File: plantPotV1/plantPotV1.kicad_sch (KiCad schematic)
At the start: 3 parts, among them U1 DS18B20

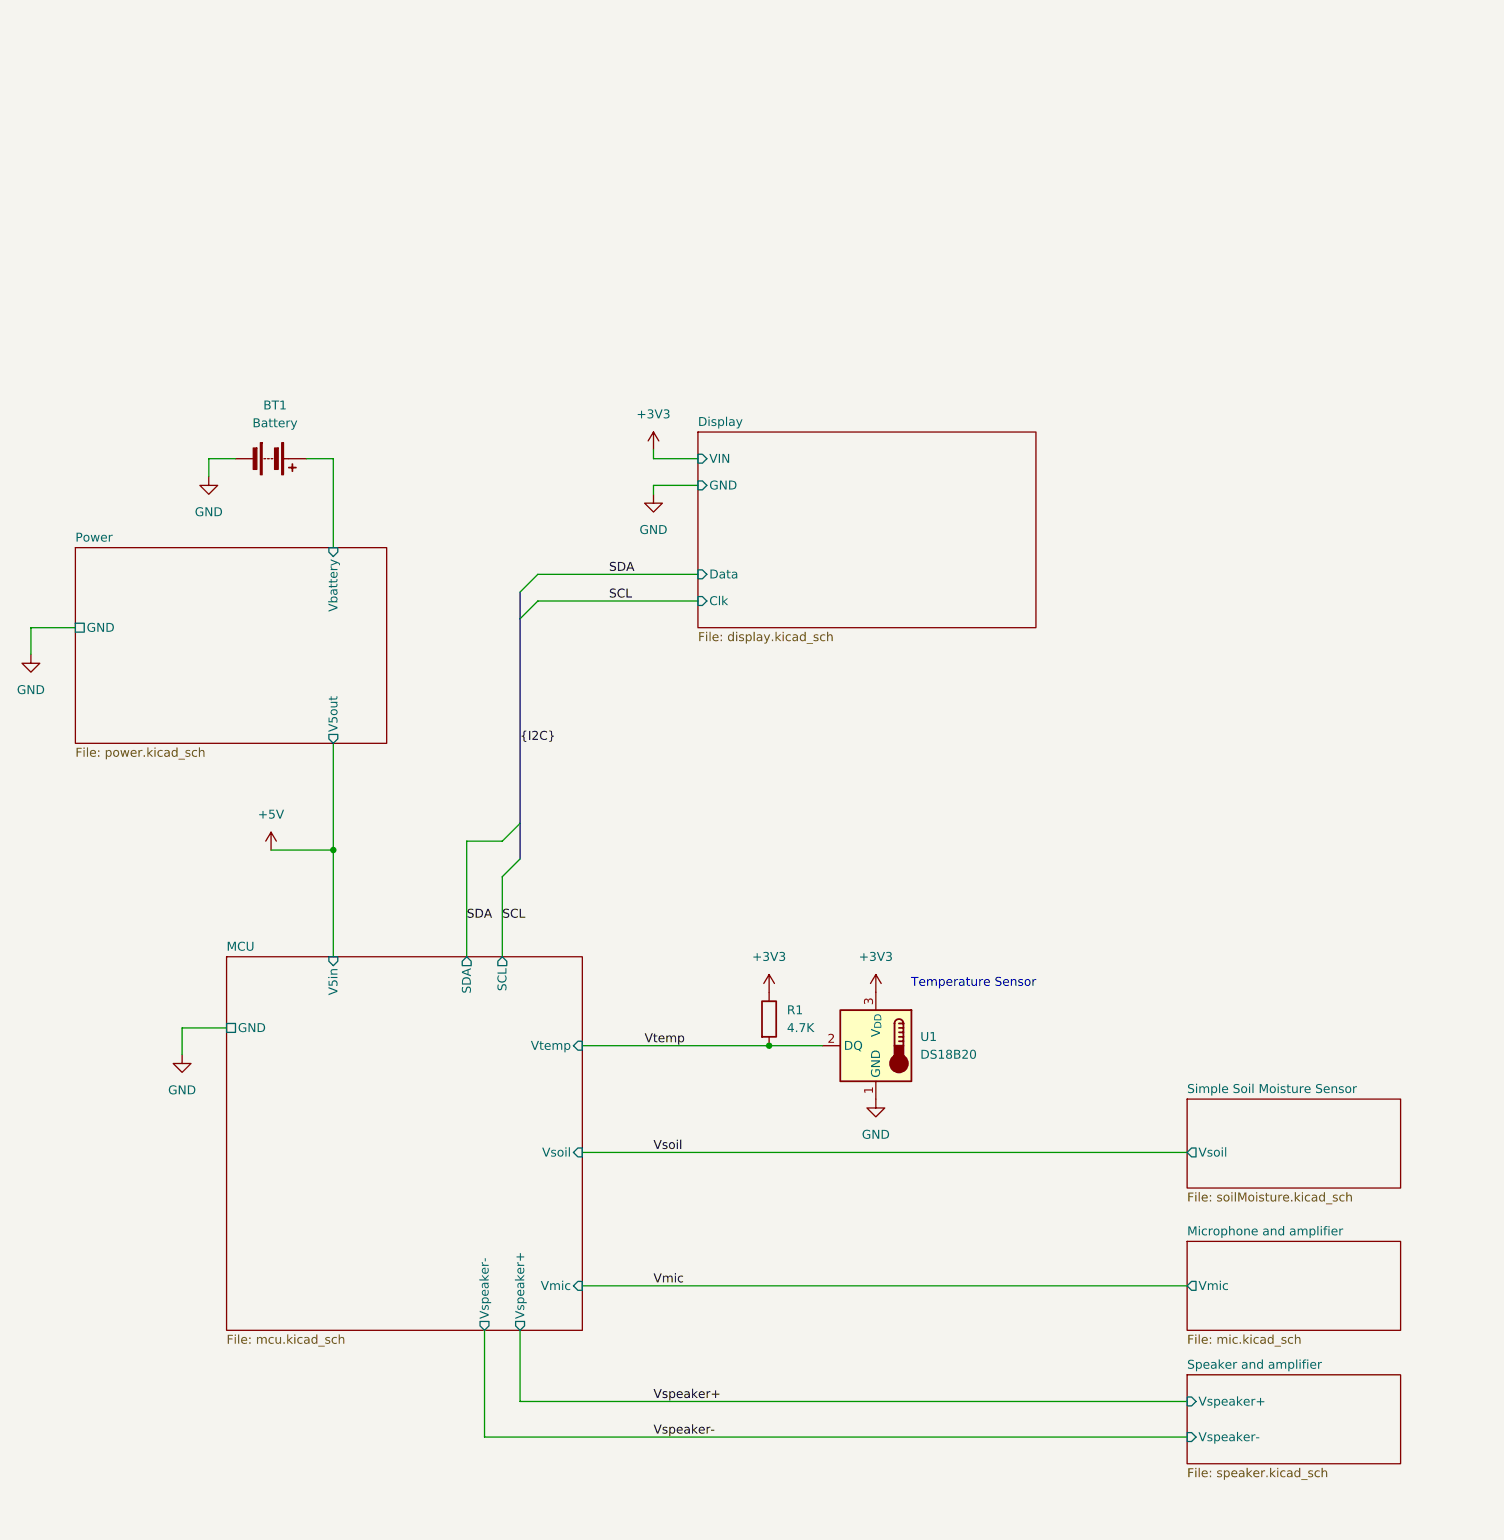
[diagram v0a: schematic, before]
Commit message: changed to meet proposal
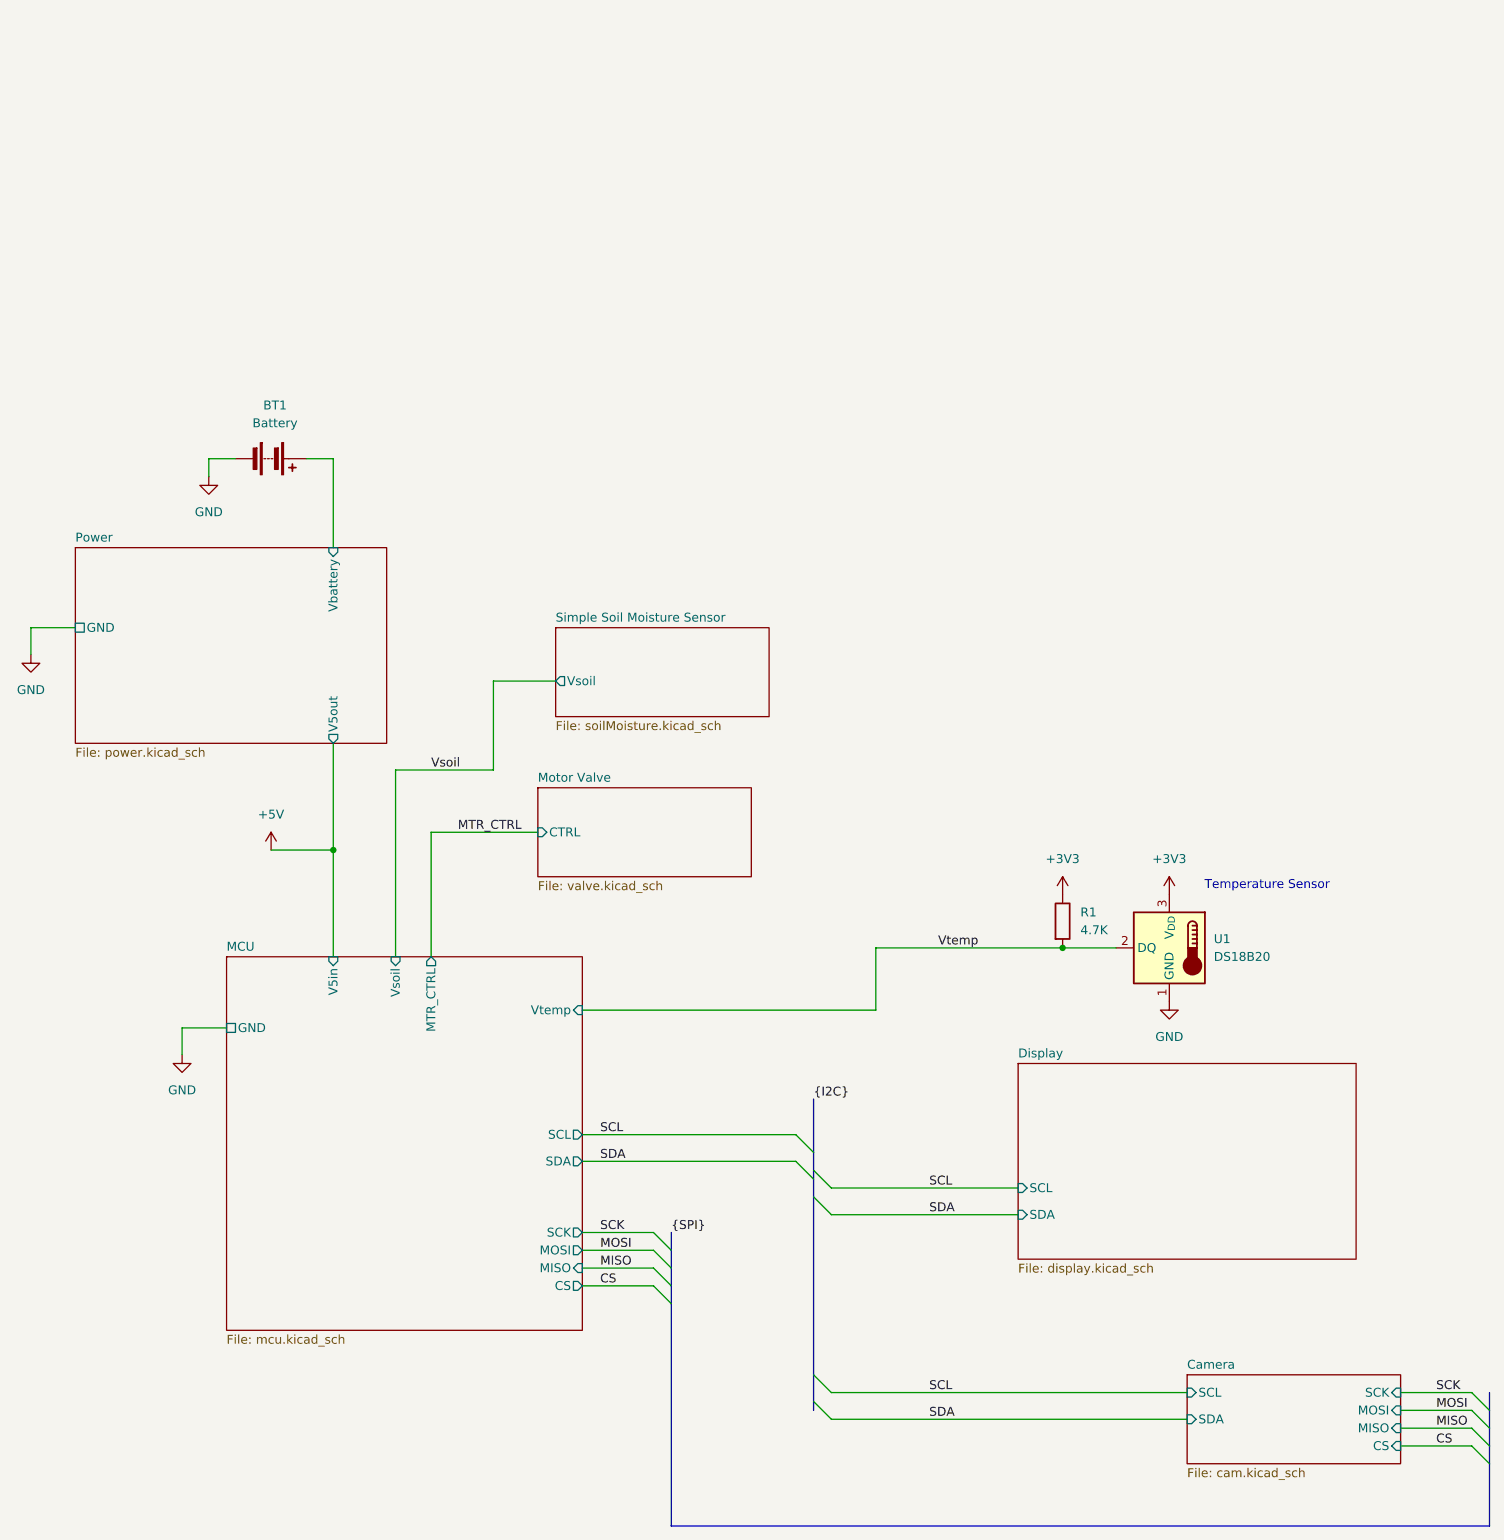
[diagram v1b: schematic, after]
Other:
- sheet Microphone and amplifier renamed Motor Valve
- sheet Speaker and amplifier renamed Camera
- sheet Camera: file speaker.kicad_sch -> cam.kicad_sch
- sheet Camera ports: added CS, MISO, MOSI, SCK, SCL, SDA; removed Vspeaker+, Vspeaker-
- sheet Display ports: added SCL, SDA; removed Clk, Data, GND, VIN
- sheet MCU ports: added CS, MISO, MOSI, MTR_CTRL, SCK; removed Vmic, Vspeaker+, Vspeaker-
- sheet Motor Valve: file mic.kicad_sch -> valve.kicad_sch
- sheet Motor Valve ports: added CTRL; removed Vmic
- moved on the sheet: R1, U1

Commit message: updated circuit diagram (top only)
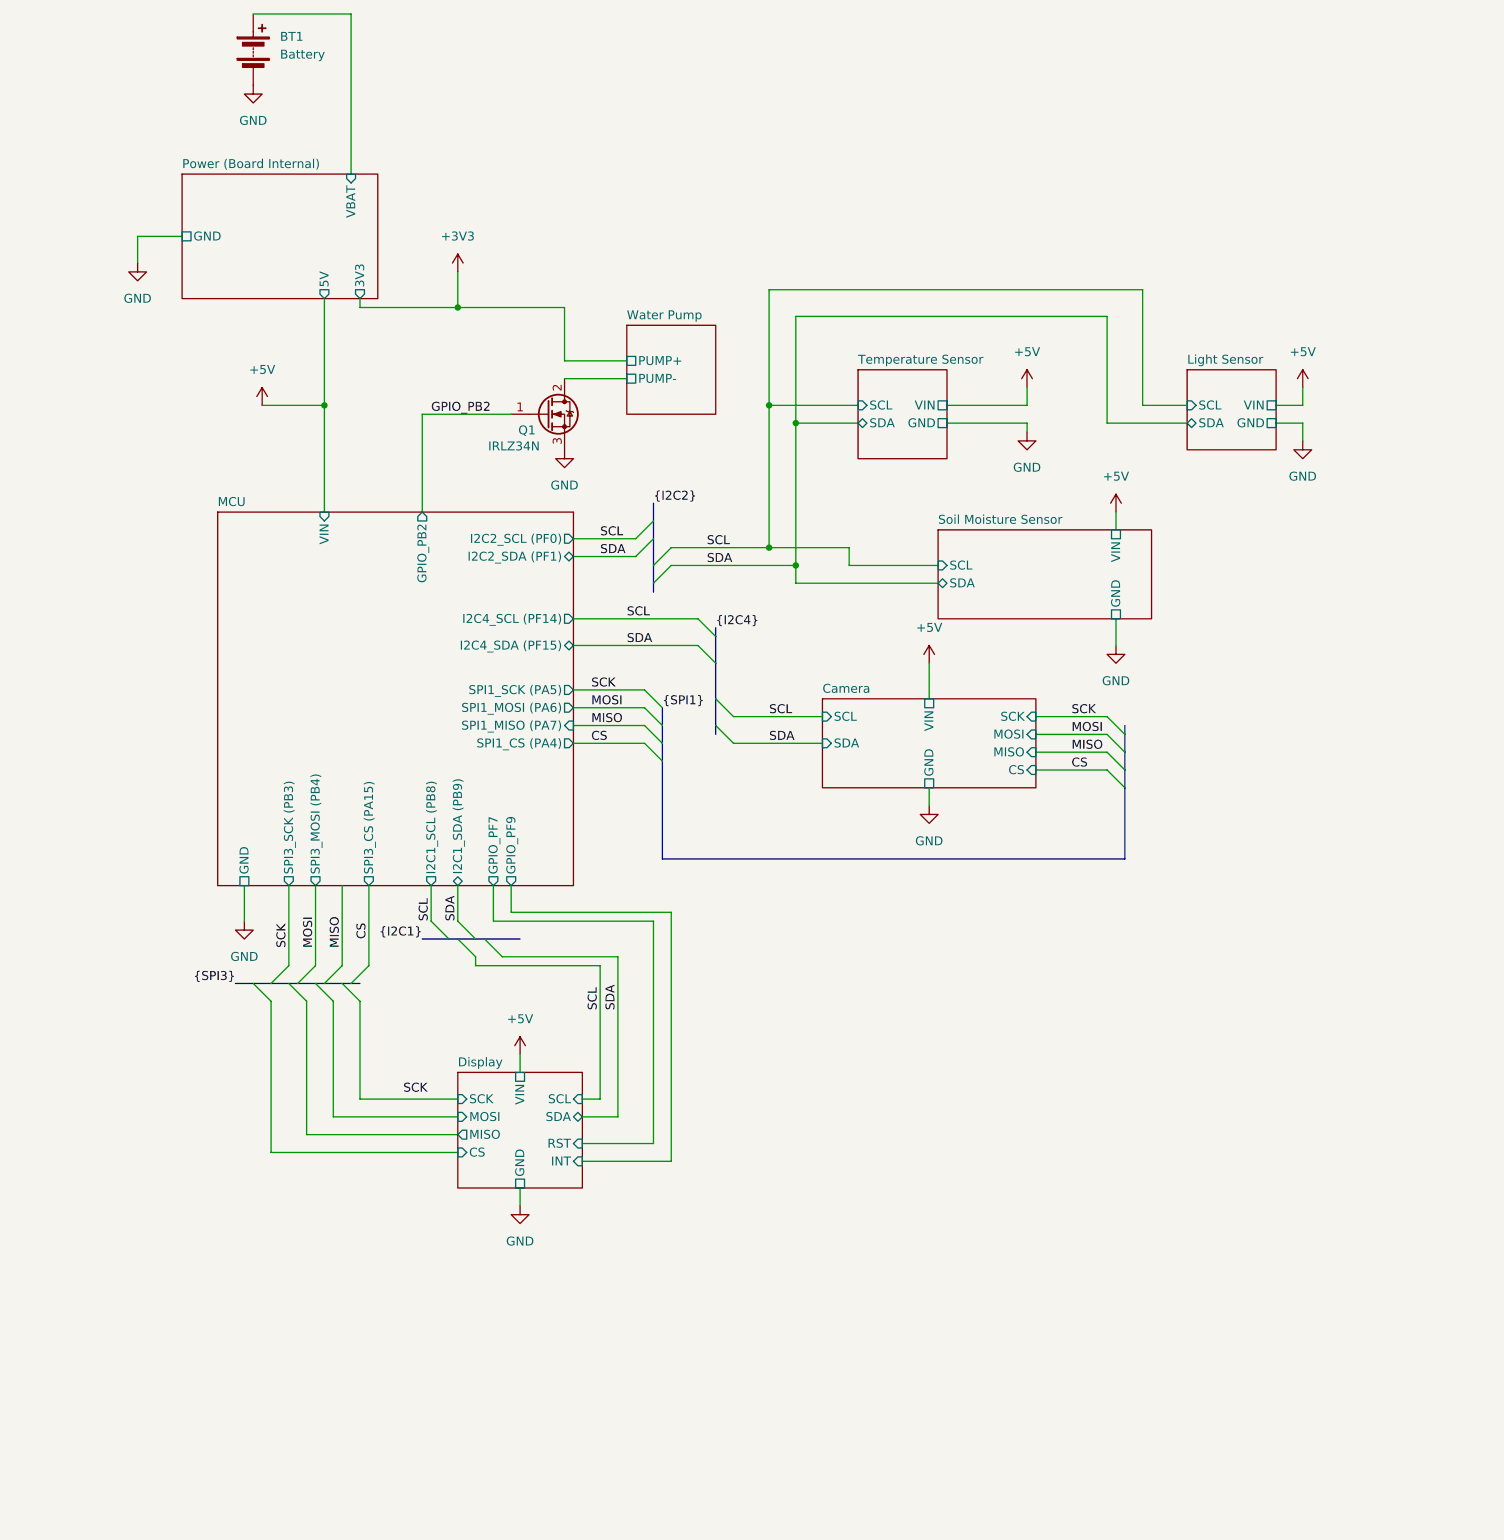
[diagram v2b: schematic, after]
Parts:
- removed R1: 4.7K, symbol Device:R
- removed U1: DS18B20, Package_TO_SOT_THT:TO-92_Inline, symbol Sensor_Temperature:DS18B20
- added Q1: IRLZ34N, Package_TO_SOT_THT:TO-220-3_Vertical, symbol Transistor_FET:IRLZ34N
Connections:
- net GND: now also Q1.3 (S)
- net Power (Board Internal)/Vbattery renamed Power (Board Internal)/VBAT
- new net GPIO_PB2: Q1.1 (G)
- new net Water Pump/PUMP-: Q1.2 (D)
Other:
- sheet Motor Valve renamed Water Pump
- sheet Power renamed Power (Board Internal)
- sheet Simple Soil Moisture Sensor renamed Soil Moisture Sensor
- added sheet Light Sensor (lightsensor.kicad_sch)
- added sheet Temperature Sensor (tempsensor.kicad_sch)
- sheet Camera ports: added GND, VIN; removed none
- sheet Display ports: added CS, GND, INT, MISO, MOSI, RST, SCK, VIN; removed none
- sheet MCU ports: added GPIO_PB2, GPIO_PF7, GPIO_PF9, I2C1_SCL (PB8), I2C1_SDA (PB9), I2C2_SCL (PF0), I2C2_SDA (PF1), I2C4_SCL (PF14), I2C4_SDA (PF15), SPI1_CS (PA4), SPI1_MISO (PA7), SPI1_MOSI (PA6), SPI1_SCK (PA5), SPI3_CS (PA15), SPI3_MOSI (PB4), SPI3_SCK (PB3), VIN; removed CS, MISO, MOSI, MTR_CTRL, SCK, SCL, SDA, V5in, Vsoil, Vtemp
- sheet Power (Board Internal) ports: added 3V3, 5V, VBAT; removed V5out, Vbattery
- sheet Soil Moisture Sensor ports: added GND, SCL, SDA, VIN; removed Vsoil
- sheet Water Pump: file valve.kicad_sch -> pump.kicad_sch
- sheet Water Pump ports: added PUMP+, PUMP-; removed CTRL
- note removed: "Temperature Sensor"
- moved on the sheet: BT1

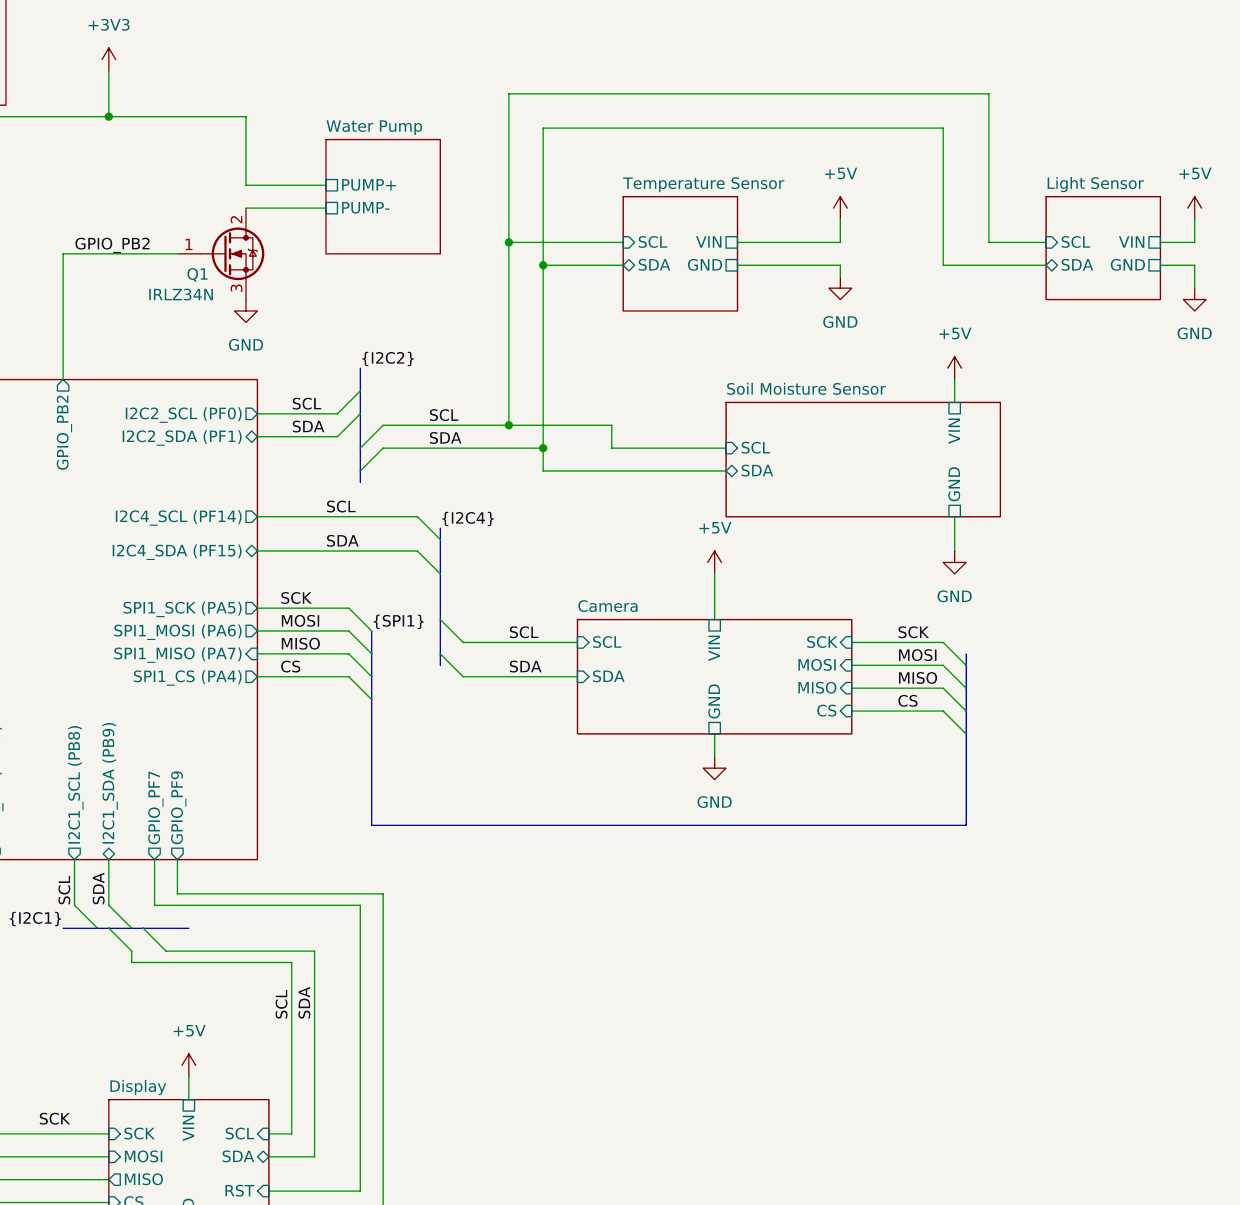
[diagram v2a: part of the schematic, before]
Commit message: update power inputs on schematic
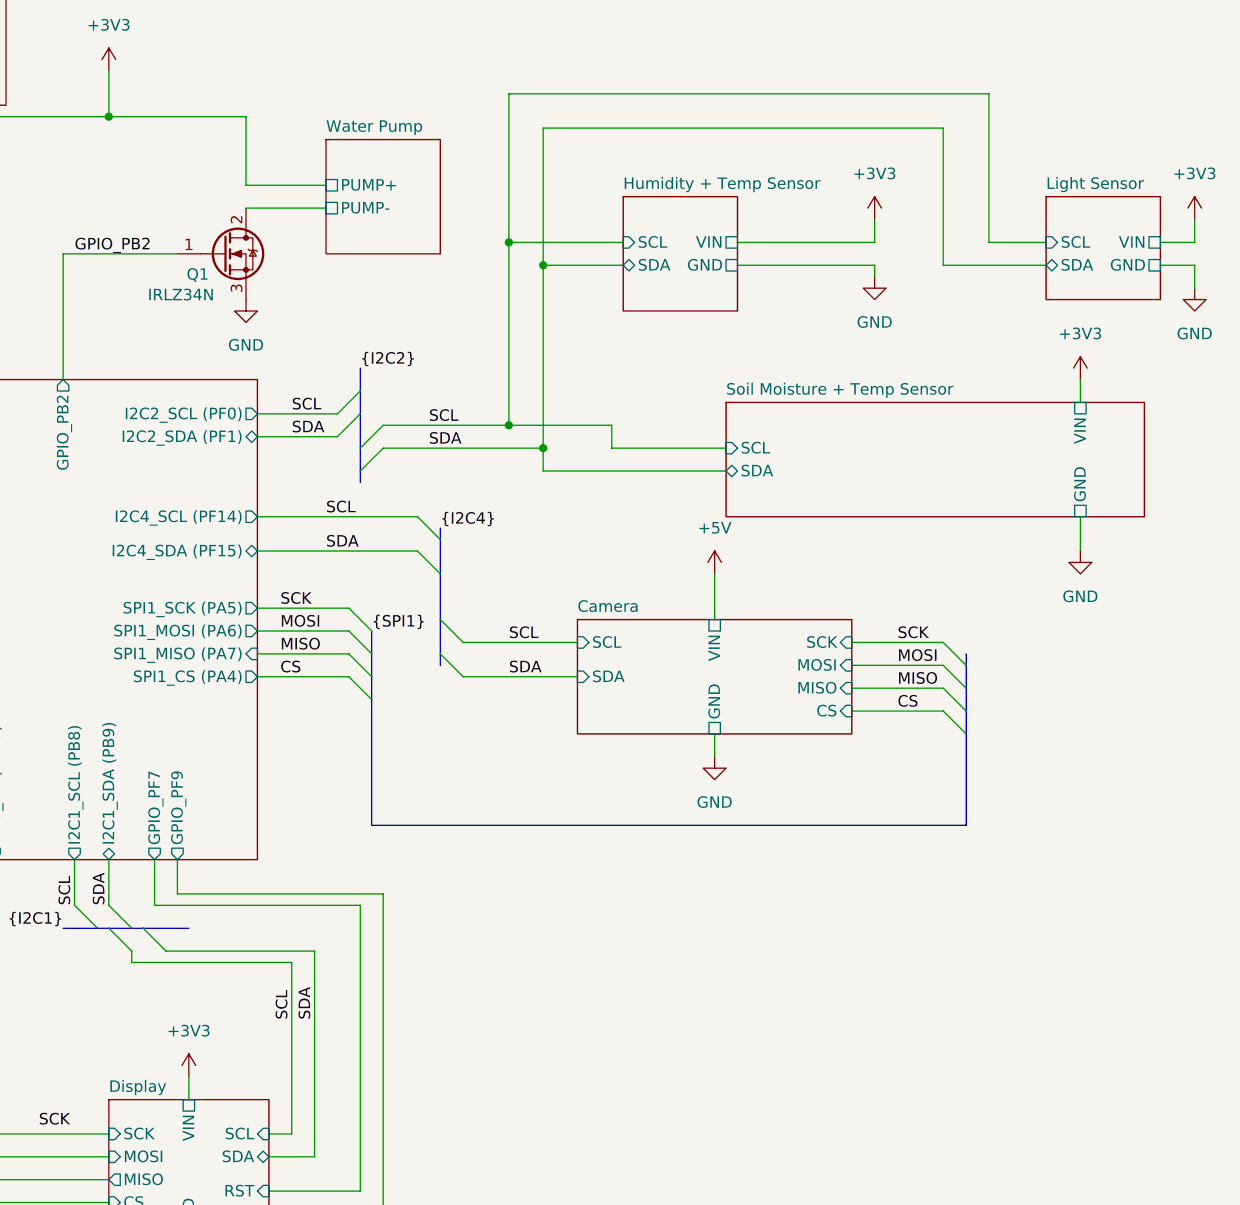
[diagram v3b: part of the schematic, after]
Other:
- sheet Soil Moisture Sensor renamed Soil Moisture + Temp Sensor
- sheet Temperature Sensor renamed Humidity + Temp Sensor
